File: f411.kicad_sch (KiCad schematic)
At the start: 16 parts, among them J18 THTPad, J21 Conn_2x02_Pin, SW1 SW_Push, SW2 SW_Push, U5 STM32F411CEUx

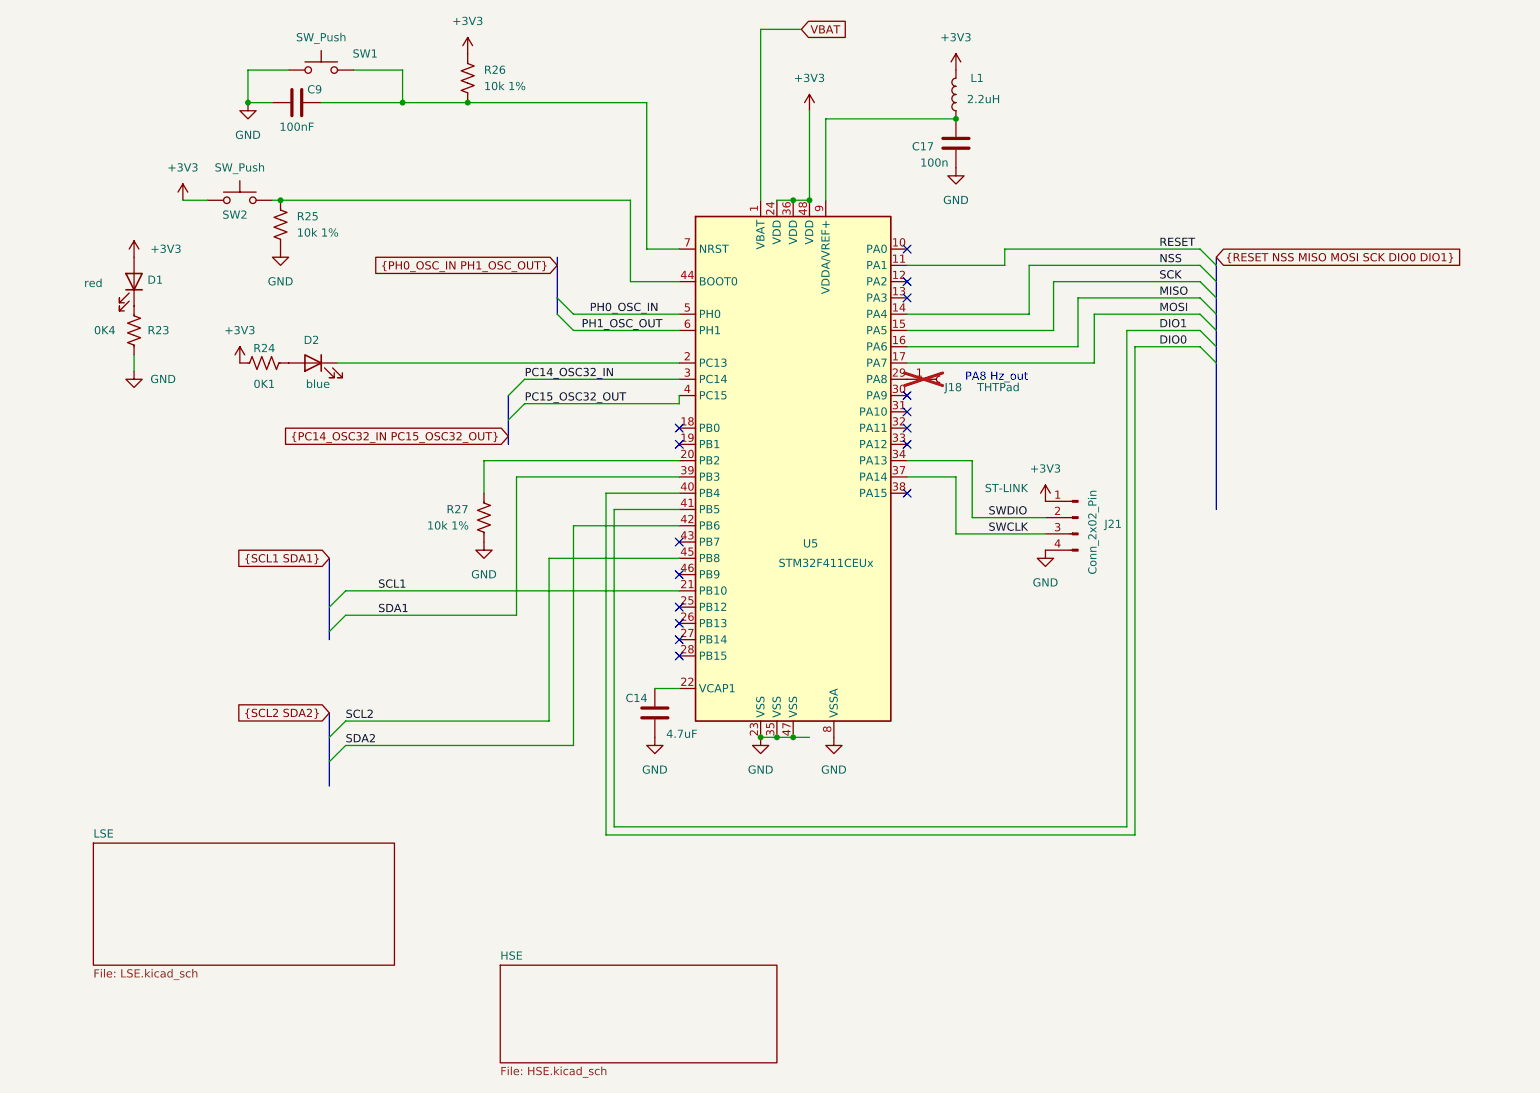
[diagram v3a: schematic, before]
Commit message: near complete, DRC good, ERC has a spurious error about ground on Y1.
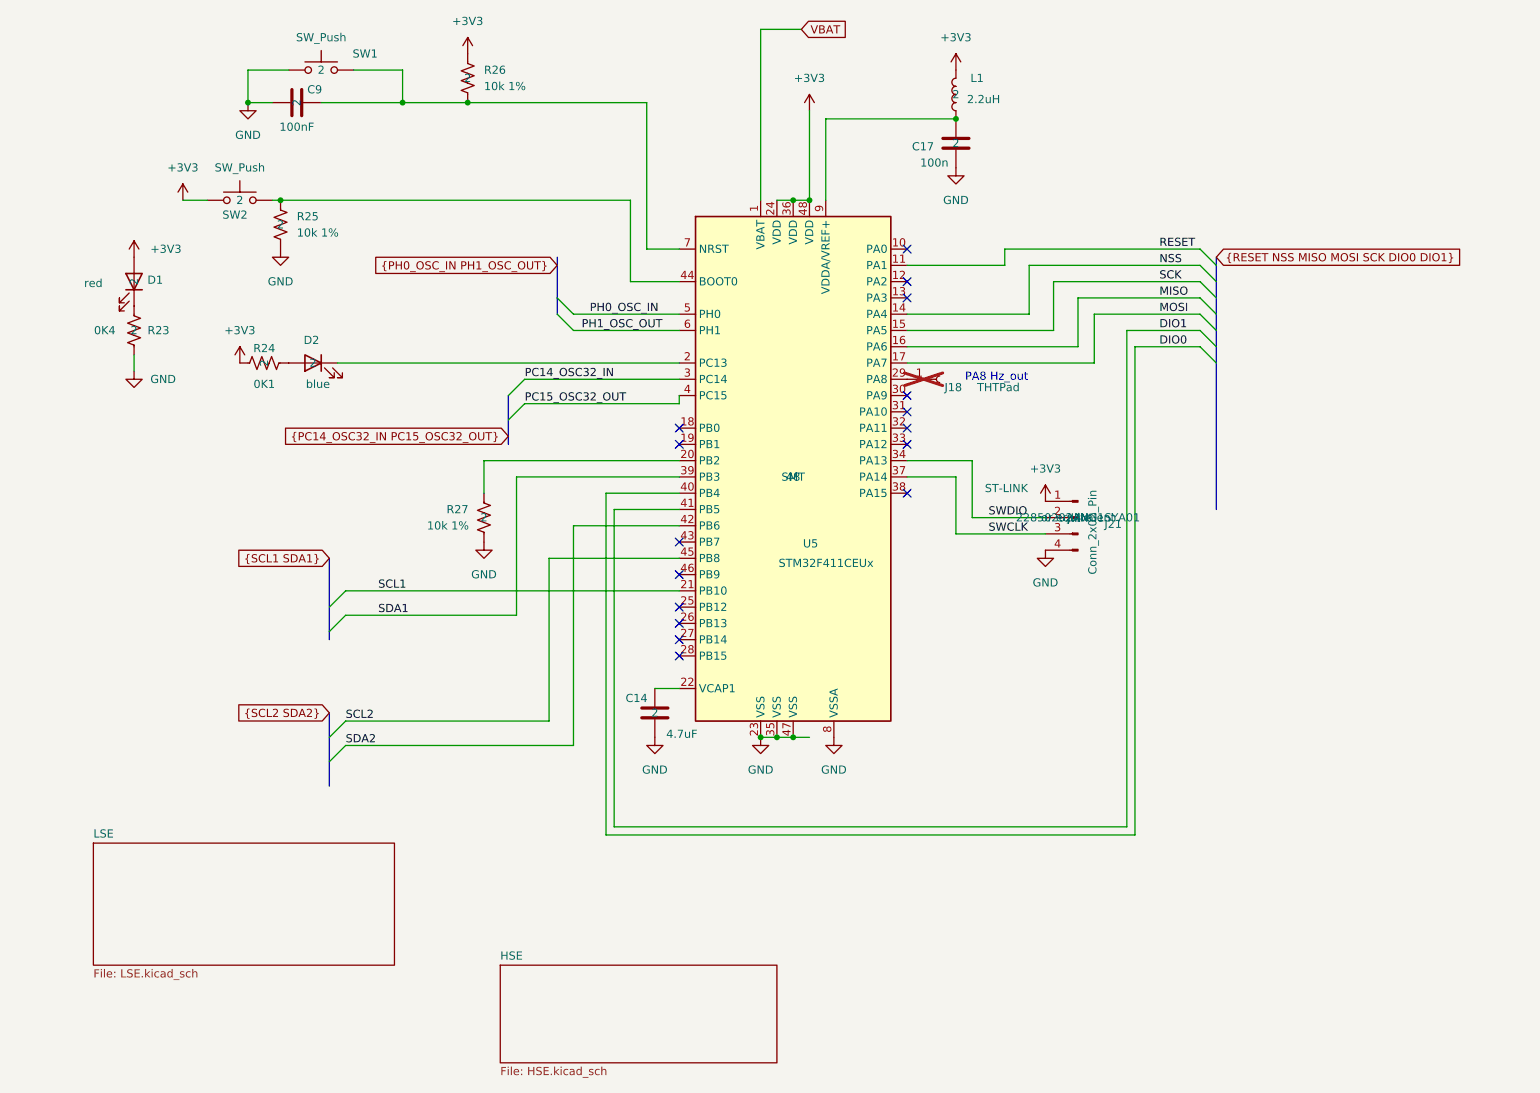
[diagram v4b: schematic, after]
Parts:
- C14, C17, C9, D1, D2, L1, R23, R24, R25, R26, R27, SW1, SW2: pads (none) -> 2
- J18: now left out of the parts list
- J21: Manufacturer (none) -> JILN; MfgPart (none) -> 22850202ANG1SYA01; Notes (none) -> or equivalent; pads (none) -> 4
- U5: MountType (none) -> SMT; pads (none) -> 48
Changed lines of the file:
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@@
+			)
+		)
+		(property "pads" "2"
+			(at 64.77 63.5 0)
+			(effects
+				(font
+					(size 1.27 1.27)
+				)
 			)
 		)
@@
 		(unit 1)
 		(exclude_from_sim no)
-		(in_bom yes)
+		(in_bom no)
 		(on_board yes)
 		(dnp yes)
@@
 			)
 		)
+		(property "pads" ""
+			(at 167.64 87.63 0)
+			(effects
+				(font
+					(size 1.27 1.27)
+				)
+			)
+		)
 		(pin "1"
 		)
@@
 			)
 		)
-		(property "Datasheet" "~"
+		(property "Datasheet" "https://www.lcsc.com/datasheet/lcsc_datasheet_2411111206_JILN-22850210ANG1SYA01_C41431943.pdf"
 			(at 189.23 109.22 0)
 			(effects
@@
 			)
 		)
-		(property "Description" "Generic connector, single row, 01x04, script generated"
+		(property "Description" "PinSocket header 2x02  4P"
 			(at 189.23 109.22 0)
 			(effects
@@
 		(property "Note" "ST-LINK"
 			(at 178.054 104.648 0)
+			(effects
+				(font
+					(size 1.27 1.27)
+				)
+			)
+		)
+		(property "Manufacturer" "JILN"
+			(at 189.23 109.22 0)
+			(effects
+				(font
+					(size 1.27 1.27)
+				)
+			)
+		)
+		(property "MfgPart" "22850202ANG1SYA01"
+			(at 189.23 109.22 0)
+			(effects
+				(font
+					(size 1.27 1.27)
+				)
+			)
+		)
+		(property "Notes" "or equivalent"
+			(at 189.23 109.22 0)
+			(effects
+				(font
+					(size 1.27 1.27)
+				)
+			)
+		)
+		(property "pads" "4"
+			(at 189.23 109.22 0)
 			(effects
 				(font
@@
 			)
 		)
+		(property "pads" "2"
+			(at 123.19 139.7 0)
+			(effects
+				(font
+					(size 1.27 1.27)
+				)
+			)
+		)
 		(pin "1"
 		)
@@
 			)
 		)
+		(property "pads" "2"
+			(at 69.85 85.09 0)
+			(effects
+				(font
+					(size 1.27 1.27)
+				)
+			)
+		)
 		(pin "1"
 		)
@@
 			)
 		)
+		(property "pads" "2"
+			(at 96.52 109.22 0)
+			(effects
+				(font
+					(size 1.27 1.27)
+				)
+			)
+		)
 		(pin "1"
 		)
@@
 			)
 		)
+		(property "pads" "2"
+			(at 67.31 44.45 0)
+			(effects
+				(font
+					(size 1.27 1.27)
+				)
+			)
+		)
 		(pin "1"
 		)
@@
 			)
 		)
+		(property "pads" "2"
+			(at 58.42 59.69 0)
+			(effects
+				(font
+					(size 1.27 1.27)
+				)
+			)
+		)
 		(pin "1"
 		)
@@
 			)
 		)
+		(property "pads" "2"
+			(at 170.18 50.8 0)
+			(effects
+				(font
+					(size 1.27 1.27)
+				)
+			)
+		)
 		(pin "1"
 		)
@@
 			)
 		)
+		(property "pads" "2"
+			(at 71.12 39.37 0)
+			(effects
+				(font
+					(size 1.27 1.27)
+				)
+			)
+		)
 		(pin "1"
 		)
@@
 				)
 				(hide yes)
+			)
+		)
+		(property "MountType" "SMT"
+			(at 144.78 102.87 0)
+			(effects
+				(font
+					(size 1.27 1.27)
+				)
+			)
+		)
+		(property "pads" "48"
+			(at 144.78 102.87 0)
+			(effects
+				(font
+					(size 1.27 1.27)
+				)
 			)
 		)
@@
 			)
 		)
+		(property "pads" "2"
+			(at 170.18 43.18 0)
+			(effects
+				(font
+					(size 1.27 1.27)
+				)
+			)
+		)
 		(pin "2"
 		)
@@
 			)
 		)
+		(property "pads" "2"
+			(at 41.91 72.39 0)
+			(effects
+				(font
+					(size 1.27 1.27)
+				)
+			)
+		)
 		(pin "1"
 		)
@@
 			)
 		)
+		(property "pads" "2"
+			(at 93.98 40.64 0)
+			(effects
+				(font
+					(size 1.27 1.27)
+				)
+			)
+		)
 		(pin "2"
 		)
@@
 			)
 		)
+		(property "pads" "2"
+			(at 62.23 85.09 0)
+			(effects
+				(font
+					(size 1.27 1.27)
+				)
+			)
+		)
 		(pin "1"
 		)
@@
 			)
 		)
+		(property "pads" "2"
+			(at 41.91 80.01 0)
+			(effects
+				(font
+					(size 1.27 1.27)
+				)
+			)
+		)

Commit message: cleanup, ready to submit.
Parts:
- C14: value 4.7uF -> 4.7µF
- C17: value 100n -> 100nF
- R23: value 0K4 -> 400
- R24: value 0K1 -> 100
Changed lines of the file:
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@@
 					(size 1.27 1.27)
 				)
+				(hide yes)
 			)
 		)
@@
 		(dnp yes)
 		(property "Reference" "J18"
-			(at 168.402 88.9 0)
+			(at 172.974 89.408 0)
 			(effects
 				(font
@@
 		)
 		(property "Value" "THTPad"
-			(at 173.482 88.9 0)
+			(at 177.546 89.154 0)
 			(effects
 				(font
@@
 					(size 1.27 1.27)
 				)
+				(hide yes)
 			)
 		)
@@
 					(size 1.27 1.27)
 				)
+				(hide yes)
 			)
 		)
@@
 					(size 1.27 1.27)
 				)
+				(hide yes)
 			)
 		)
@@
 					(size 1.27 1.27)
 				)
+				(hide yes)
 			)
 		)
@@
 			)
 		)
-		(property "Value" "4.7uF"
+		(property "Value" "4.7µF"
 			(at 124.968 143.002 0)
 			(effects
@@
 					(size 1.27 1.27)
 				)
+				(hide yes)
 			)
 		)
@@
 					(size 1.27 1.27)
 				)
+				(hide yes)
 			)
 		)
@@
 					(size 1.27 1.27)
 				)
+				(hide yes)
 			)
 		)
@@
 					(size 1.27 1.27)
 				)
+				(hide yes)
 			)
 		)
@@
 					(size 1.27 1.27)
 				)
+				(hide yes)
 			)
 		)
@@
 			)
 		)
-		(property "Value" "100n"
-			(at 164.592 53.848 0)
+		(property "Value" "100nF"
+			(at 162.814 54.102 0)
 			(effects
 				(font
@@
 					(size 1.27 1.27)
 				)
+				(hide yes)
 			)
 		)
@@
 					(size 1.27 1.27)
 				)
+				(hide yes)
 			)
 		)
@@
 			)
 		)
-		(property "Description" "STMicroelectronics Arm Cortex-M4 MCU, 512KB flash, 128KB RAM, 100 MHz, 1.7-3.6V, 36 GPIO, UFQFPN48"
+		(property "Description" "Arm Cortex-M4 MCU, 512KB flash, 128KB RAM,  1.7-3.6V, UFQFPN48"
 			(at 144.78 102.87 0)
 			(effects
@@
 					(size 1.27 1.27)
 				)
+				(hide yes)
 			)
 		)
@@
 					(size 1.27 1.27)
 				)
+				(hide yes)
 			)
 		)
@@
 					(size 1.27 1.27)
 				)
+				(hide yes)
 			)
 		)
@@
 			)
 		)
-		(property "Value" "0K1"
+		(property "Value" "100"
 			(at 62.23 88.392 90)
 			(effects
@@
 					(size 1.27 1.27)
 				)
+				(hide yes)
 			)
 		)
@@
 			)
 		)
-		(property "Value" "0K4"
+		(property "Value" "400"
 			(at 37.338 80.01 0)
 			(effects
@@
 					(size 1.27 1.27)
 				)
-			)
-		)
+				(hide yes)
+			)
+		)
